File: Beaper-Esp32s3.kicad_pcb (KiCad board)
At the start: 2 copper layers, 65.5 x 100 mm, 98 parts, among them CON1 Phoenix 1729160, J1 Digital, J2 Analog, J3 Conn_01x08, J4 QWIIC/JST SH, Q1 LTR-4206E, Q2 LTR-4206E, Q3 LTR-4206E, Q4 TEPT4400, SW1 RESET, SW2 SW_Push, SW3 SW_Push, SW4 SW_Push, SW5 SW_Push, U1 LM2940T-5.0, U2 74HCT541, U3 SN754410NE, U4 MCP9700A-E/TO

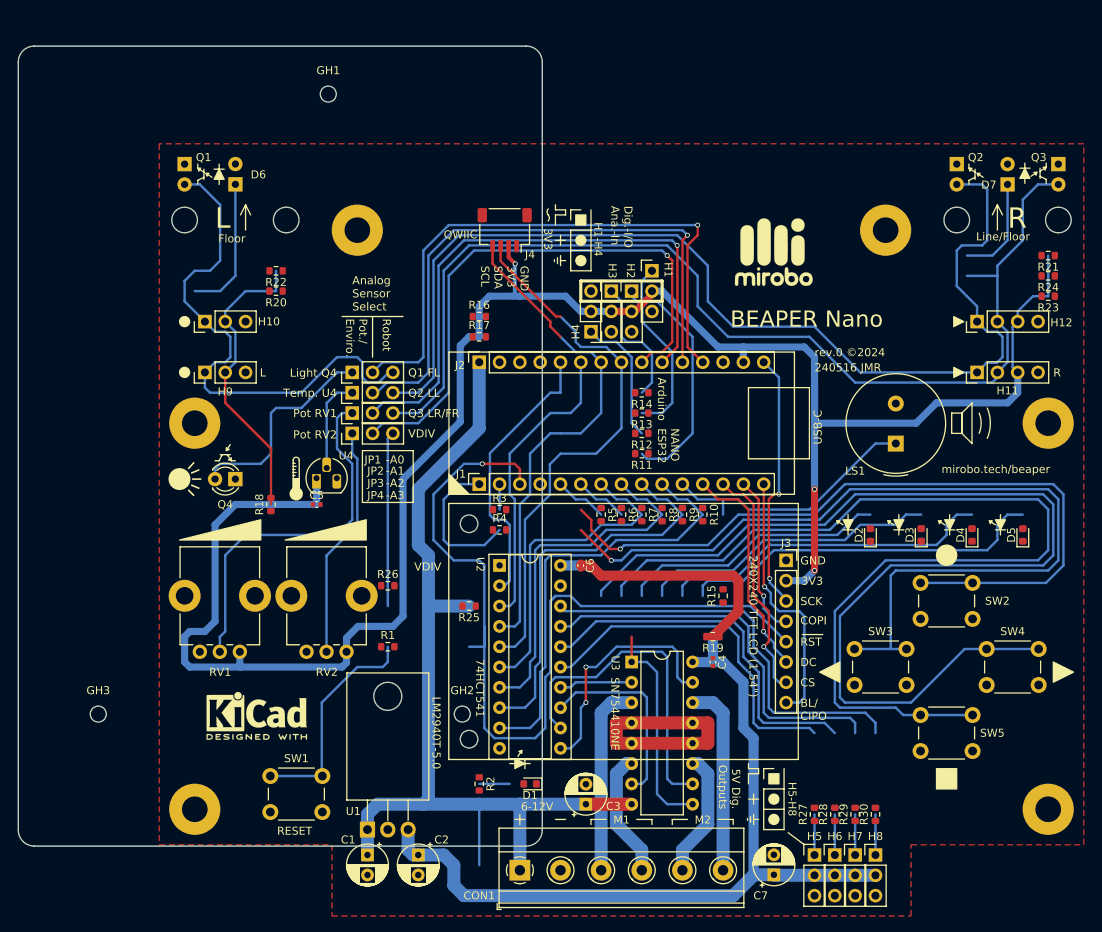
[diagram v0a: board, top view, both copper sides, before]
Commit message: Ajout des jst-ph, ajustement des positions, headers i2c
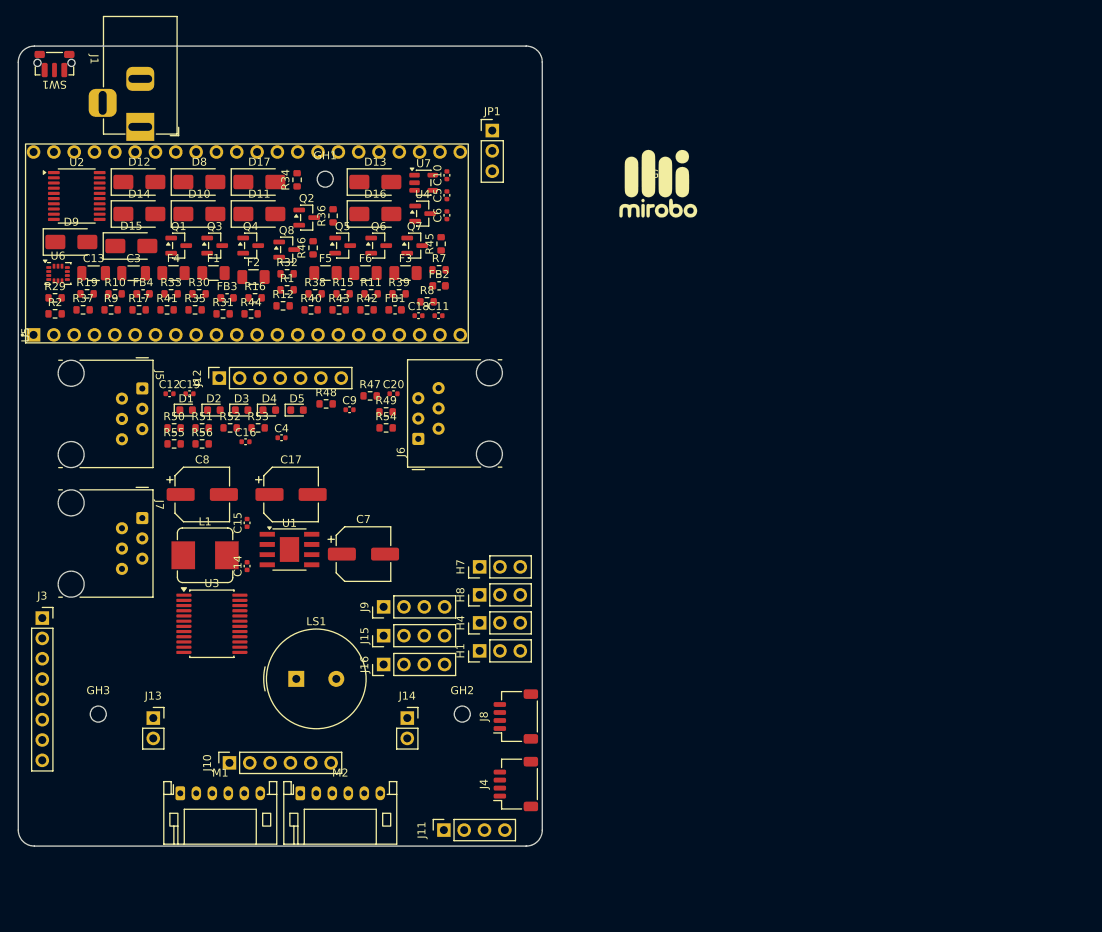
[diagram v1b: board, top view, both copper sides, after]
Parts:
- removed C1, C2: 10uF, Capacitor_THT:CP_Radial_D5.0mm_P2.50mm
- removed CON1: Phoenix 1729160, TerminalBlock_Phoenix:TerminalBlock_Phoenix_MKDS-1,5-6-5.08_1x06_P5.08mm_Horizontal
- removed D6, D7: OED-EL-1L2, BEAPER-Nano:LED_D5.0mm_Clear
- removed H10, H9: Conn_01x03_Male, Connector_PinHeader_2.54mm:PinHeader_1x03_P2.54mm_Vertical
- removed H11, H12: Conn_01x04_Pin, Connector_PinHeader_2.54mm:PinHeader_1x04_P2.54mm_Vertical
- removed H2: A6 (SONAR TRIG), Connector_PinHeader_2.54mm:PinHeader_1x03_P2.54mm_Vertical
- removed H3: A7 (SONAR ECHO), Connector_PinHeader_2.54mm:PinHeader_1x03_P2.54mm_Vertical
- removed H5: A4 (Servo 1), Connector_PinHeader_2.54mm:PinHeader_1x03_P2.54mm_Vertical
- removed H6: A5 (Servo 2), Connector_PinHeader_2.54mm:PinHeader_1x03_P2.54mm_Vertical
- removed J2: Analog, Connector_PinSocket_2.54mm:PinSocket_1x15_P2.54mm_Vertical
- removed JP2: ALS/LFS, Connector_PinHeader_2.54mm:PinHeader_1x03_P2.54mm_Vertical
- removed JP3, JP4: POT/VDIV, Connector_PinHeader_2.54mm:PinHeader_1x03_P2.54mm_Vertical
- removed R13, R14, R20, R21, R27, R28: 100, Resistor_SMD:R_0603_1608Metric
- removed R18, R22, R23, R24: 4k7, Resistor_SMD:R_0603_1608Metric
- removed R25: 5.62k-1%, Resistor_SMD:R_0603_1608Metric
- removed R26: 1.37k-1%, Resistor_SMD:R_0603_1608Metric
- removed R3, R4, R5, R6: 1k0, Resistor_SMD:R_0603_1608Metric
- removed REF**: KiCad-Logo2_5mm_SilkScreen, Symbol:KiCad-Logo2_5mm_SilkScreen
- removed REF** (x6): MountingHole_3.2mm_M3_Pad, MountingHole:MountingHole_3.2mm_M3_Pad
- removed REF** (x4): MountingHole_3.2mm_M3, MountingHole:MountingHole_3.2mm_M3
- removed REF** (x2): MountingHole_2.2mm_M2, MountingHole:MountingHole_2.2mm_M2
- removed RV1, RV2: 10k, Potentiometer_THT:Potentiometer_Bourns_PTV09A-1_Single_Vertical
- removed SW2, SW3, SW4, SW5: SW_Push, Button_Switch_THT:SW_PUSH_6mm
- added C10: 100nF, Capacitor_SMD:C_0402_1005Metric, F.Cu at (103.6, 46.1)
- added C11: 1uF, Capacitor_SMD:C_0402_1005Metric, F.Cu at (102.5, 63.7)
- added C12: 100nF, Capacitor_SMD:C_0402_1005Metric, F.Cu at (68.9, 73.5)
- added C13: 10uF/50V, Capacitor_SMD:C_1206_3216Metric, F.Cu at (59.4, 58.4)
- added C14: 100nF, Capacitor_SMD:C_0402_1005Metric, F.Cu at (78.6, 95.0)
- added C15: 100nF, Capacitor_SMD:C_0402_1005Metric, F.Cu at (78.6, 89.6)
- added C16: 10nF, Capacitor_SMD:C_0402_1005Metric, F.Cu at (78.4, 79.5)
- added C17: 470uF/16V, Capacitor_SMD:CP_Elec_6.3x7.7, F.Cu at (84.1, 86.0)
- added C18: 100nF, Capacitor_SMD:C_0402_1005Metric, F.Cu at (100.0, 63.7)
- added C19: 120pF, Capacitor_SMD:C_0402_1005Metric, F.Cu at (71.4, 73.5)
- added C20: 68pF, Capacitor_SMD:C_0402_1005Metric, F.Cu at (96.9, 73.5)
- added C8: 470uF/16V, Capacitor_SMD:CP_Elec_6.3x7.7, F.Cu at (73.0, 86.0)
- added C9: 100nF, Capacitor_SMD:C_0402_1005Metric, F.Cu at (91.4, 75.5)
- added D10: SS34, Diode_SMD:D_SMA, F.Cu at (72.6, 51.0)
- added D11: SS34, Diode_SMD:D_SMA, F.Cu at (80.1, 51.0)
- added D12: SMAJ5.0CA, Diode_SMD:D_SMA, F.Cu at (65.1, 47.0)
- added D13: SS34, Diode_SMD:D_SMA, F.Cu at (94.6, 47.0)
- added D14: SMAJ12CA, Diode_SMD:D_SMA, F.Cu at (65.1, 51.0)
- added D15: SMAJ12CA, Diode_SMD:D_SMA, F.Cu at (64.1, 55.0)
- added D16: SMAJ12CA, Diode_SMD:D_SMA, F.Cu at (94.6, 51.0)
- added D17: SMAJ12CA, Diode_SMD:D_SMA, F.Cu at (80.1, 47.0)
- added D8: SS54, Diode_SMD:D_SMA, F.Cu at (72.6, 47.0)
- added D9: SMAJ13CA, Diode_SMD:D_SMA, F.Cu at (56.6, 54.5)
- added F1: 3.5A, Fuse:Fuse_1206_3216Metric, F.Cu at (74.4, 58.4)
- added F2: 3A, Fuse:Fuse_1206_3216Metric, F.Cu at (79.4, 58.9)
- added F3: 1A PTC, Fuse:Fuse_1206_3216Metric, F.Cu at (98.4, 58.4)
- added F4: 1A PTC, Fuse:Fuse_1206_3216Metric, F.Cu at (69.4, 58.4)
- added F5: 1A PTC, Fuse:Fuse_1206_3216Metric, F.Cu at (88.4, 58.4)
- added F6: 1A PTC, Fuse:Fuse_1206_3216Metric, F.Cu at (93.4, 58.4)
- added FB1: 120R/2A, Inductor_SMD:L_0603_1608Metric, F.Cu at (97.1, 63.0)
- added FB2: 120R/2A, Inductor_SMD:L_0603_1608Metric, F.Cu at (102.6, 60.0)
- added FB3: 120R/2A, Inductor_SMD:L_0603_1608Metric, F.Cu at (76.1, 61.5)
- added FB4: 120R/2A, Inductor_SMD:L_0603_1608Metric, F.Cu at (65.6, 61.0)
- added J10: VL53L1X module, Connector_PinSocket_2.54mm:PinSocket_1x06_P2.54mm_Vertical, F.Cu at (76.4, 119.6)
- added J11: OLED I2C, Connector_PinSocket_2.54mm:PinSocket_1x04_P2.54mm_Vertical, F.Cu at (103.2, 128.0)
- added J12: PRGB (Auriga panel module), Connector_PinSocket_2.54mm:PinSocket_1x07_P2.54mm_Vertical, F.Cu at (75.1, 71.5)
- added J13: PG1 (GND support), Connector_PinSocket_2.54mm:PinSocket_1x02_P2.54mm_Vertical, F.Cu at (66.9, 114.0)
- added J14: PG2 (GND support), Connector_PinSocket_2.54mm:PinSocket_1x02_P2.54mm_Vertical, F.Cu at (98.6, 114.0)
- added J15: I2C (GND 3V3 SCL SDA), Connector_PinHeader_2.54mm:PinHeader_1x04_P2.54mm_Vertical, F.Cu at (95.7, 103.7)
- added J16: I2C (GND 3V3 SCL SDA), Connector_PinHeader_2.54mm:PinHeader_1x04_P2.54mm_Vertical, F.Cu at (95.7, 107.3)
- added J5: RJ25 port A, Connector_RJ:RJ12_Amphenol_54601-x06_Horizontal, F.Cu at (65.5, 72.8)
- added J6: RJ25 port B, Connector_RJ:RJ12_Amphenol_54601-x06_Horizontal, F.Cu at (100.0, 79.1)
- added J7: RJ25 port C, Connector_RJ:RJ12_Amphenol_54601-x06_Horizontal, F.Cu at (65.5, 89.0)
- added J8: QWIIC/JST SH, Connector_JST:JST_SH_SM04B-SRSS-TB_1x04-1MP_P1.00mm_Horizontal, F.Cu at (112.2, 113.8)
- added J9: I2C (GND 3V3 SCL SDA), Connector_PinHeader_2.54mm:PinHeader_1x04_P2.54mm_Vertical, F.Cu at (95.7, 100.1)
- added L1: 6.8uH/4.5A, Inductor_SMD:L_Bourns_SRP7028A_7.3x6.6mm, F.Cu at (73.3, 93.7)
- added M1: Moteur 1 (MHDR1X6), Connector_JST:JST_PH_S6B-PH-K_1x06_P2.00mm_Horizontal, F.Cu at (70.2, 123.4)
- added M2: Moteur 2 (MHDR1X6), Connector_JST:JST_PH_S6B-PH-K_1x06_P2.00mm_Horizontal, F.Cu at (85.2, 123.4)
- added Q5: BSS138, Package_TO_SOT_SMD:SOT-23, F.Cu at (90.5, 54.9)
- added Q6: BSS138, Package_TO_SOT_SMD:SOT-23, F.Cu at (95.0, 54.9)
- added Q7: BSS138, Package_TO_SOT_SMD:SOT-23, F.Cu at (99.5, 54.9)
- added Q8: BSS138, Package_TO_SOT_SMD:SOT-23, F.Cu at (83.5, 55.4)
- added R31: 51, Resistor_SMD:R_0603_1608Metric, F.Cu at (75.6, 63.5)
- added R32: 51, Resistor_SMD:R_0603_1608Metric, F.Cu at (83.6, 58.5)
- added R33: 51, Resistor_SMD:R_0603_1608Metric, F.Cu at (69.1, 61.0)
- added R34: 51, Resistor_SMD:R_0603_1608Metric, F.Cu at (84.8, 46.7)
- added R35: 100k, Resistor_SMD:R_0603_1608Metric, F.Cu at (72.1, 63.0)
- added R36: 51k, Resistor_SMD:R_0603_1608Metric, F.Cu at (89.3, 51.2)
- added R37: 10k, Resistor_SMD:R_0603_1608Metric, F.Cu at (58.1, 63.0)
- added R38: 15k, Resistor_SMD:R_0603_1608Metric, F.Cu at (87.1, 61.0)
- added R39: 220, Resistor_SMD:R_0603_1608Metric, F.Cu at (97.6, 61.0)
- added R40: 10k, Resistor_SMD:R_0603_1608Metric, F.Cu at (86.6, 63.0)
- added R41: 1.91k, Resistor_SMD:R_0603_1608Metric, F.Cu at (68.6, 63.0)
- added R42: 30k, Resistor_SMD:R_0603_1608Metric, F.Cu at (93.6, 63.0)
- added R43: 4.7k, Resistor_SMD:R_0603_1608Metric, F.Cu at (90.1, 63.0)
- added R44: 4.7k, Resistor_SMD:R_0603_1608Metric, F.Cu at (79.1, 63.5)
- added R45: 10k, Resistor_SMD:R_0603_1608Metric, F.Cu at (102.8, 54.7)
- added R46: 10k, Resistor_SMD:R_0603_1608Metric, F.Cu at (86.8, 55.2)
- added R47: 10k, Resistor_SMD:R_0603_1608Metric, F.Cu at (94.0, 73.7)
- added R48: 10k, Resistor_SMD:R_0603_1608Metric, F.Cu at (88.5, 74.7)
- added R49: 10k, Resistor_SMD:R_0603_1608Metric, F.Cu at (96.0, 75.7)
- added R50: 10k, Resistor_SMD:R_0603_1608Metric, F.Cu at (69.5, 77.7)
- added R51: 10k, Resistor_SMD:R_0603_1608Metric, F.Cu at (73.0, 77.7)
- added R52: 10k, Resistor_SMD:R_0603_1608Metric, F.Cu at (76.5, 77.7)
- added R53: 10k, Resistor_SMD:R_0603_1608Metric, F.Cu at (80.0, 77.7)
- added R54: 10k, Resistor_SMD:R_0603_1608Metric, F.Cu at (96.0, 77.7)
- added R55: 10k, Resistor_SMD:R_0603_1608Metric, F.Cu at (69.5, 79.7)
- added R56: 10k, Resistor_SMD:R_0603_1608Metric, F.Cu at (73.0, 79.7)
- added U5: ESP32-S3-DevKitC-1-N16R8, BEAPER-Nano:ESP32-S3-DevKitC-1, F.Cu at (51.9, 66.1)
- added U6: LSM6DS3TR-C, Package_LGA:LGA-14_3x2.5mm_P0.5mm_LayoutBorder3x4y, F.Cu at (55.0, 58.4)
- added U7: 74AHCT1G125, Package_TO_SOT_SMD:SOT-23-5, F.Cu at (100.7, 47.1)
- C3: value 10uF -> 10uF/50V; footprint Capacitor_THT:CP_Radial_D5.0mm_P2.50mm -> Capacitor_SMD:C_1206_3216Metric
- C7: value 10uF -> 470uF/16V; footprint Capacitor_THT:CP_Radial_D5.0mm_P2.50mm -> Capacitor_SMD:CP_Elec_6.3x7.7
- J1: value Digital -> DC jack 5.5x2.1; footprint Connector_PinSocket_2.54mm:PinSocket_1x15_P2.54mm_Vertical -> Connector_BarrelJack:BarrelJack_Horizontal
- JP1: value ALS/LFS -> I2C EXT 3V3/5V
- Q1, Q2, Q3: value LTR-4206E -> BSS138; footprint BEAPER-Nano:LED_D3.0mm_IRBlack -> Package_TO_SOT_SMD:SOT-23; moved to F.Cu
- Q4: value TEPT4400 -> BSS138; footprint BEAPER-Nano:LED_D3.0mm_Clear -> Package_TO_SOT_SMD:SOT-23
- SW1: footprint Button_Switch_THT:SW_PUSH_6mm -> Button_Switch_SMD:SW_Push_1P1T-MP_NO_Horizontal_Alps_SKRTLAE010
- U1: value LM2940T-5.0 -> TPS54331DDA; footprint Package_TO_SOT_THT:TO-220-3_Horizontal_TabDown -> Package_SO:TI_SO-PowerPAD-8
- U2: footprint Package_DIP:DIP-20_W7.62mm_Socket -> Package_SO:TSSOP-20_4.4x6.5mm_P0.65mm
- U3: value SN754410NE -> TB6612FNG; footprint Package_DIP:DIP-16_W7.62mm -> Package_SO:SSOP-24_5.3x8.2mm_P0.65mm
- U4: value MCP9700A-E/TO -> MCP9700AT-E/TT; footprint Package_TO_SOT_THT:TO-92_HandSolder -> Package_TO_SOT_SMD:SOT-23
- moved R29 119.0 mm to (54.6, 61.5), turned to 0 degrees
- moved R30 106.7 mm to (72.6, 61.0), turned to 0 degrees
- moved Q3 105.7 mm to (74.5, 54.9), turned to 0 degrees
- moved SW1 99.5 mm to (54.5, 32.1)
- moved J3 93.3 mm to (53.0, 101.5)
- moved D5 92.1 mm to (84.8, 75.5), turned to 0 degrees
- moved D4 89.2 mm to (81.4, 75.5), turned to 0 degrees
- moved R19 89.2 mm to (58.6, 61.0), turned to 0 degrees
- moved C3 87.2 mm to (64.4, 58.4), turned to 0 degrees
- moved D3 86.4 mm to (77.9, 75.5), turned to 0 degrees
- moved D2 83.5 mm to (74.5, 75.5), turned to 0 degrees
- moved Q2 81.4 mm to (86.0, 51.4), turned to 0 degrees
- moved LS1 80.5 mm to (84.8, 109.1), turned to 0 degrees
- moved R2 79.1 mm to (54.6, 63.5), turned to 0 degrees
- moved R10 78.5 mm to (62.1, 61.0), turned to 0 degrees
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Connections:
- J1 pad 1: /D1/TX0 -> /VBAT
- J1 pad 2: /D0/RX0 -> GND
- J1 pad 3: /~{RST} -> (no net)
- JP1 pad 1: Net-(JP1-A) -> +3V3
- JP1 pad 2: /A0 -> /VI2C
- JP1 pad 3: /Q1 -> /5V_P
- Q1 pad 1: /Q1 -> +3V3
- Q1 pad 2: GND -> /A4/SDA
- Q2 pad 1: /Q2 -> +3V3
- Q2 pad 2: GND -> /A5/SCL
- Q3 pad 1: /Q3 -> +3V3
- Q3 pad 2: GND -> /PA_S1
- Q4 pad 1: Net-(JP1-A) -> +3V3
- Q4 pad 2: GND -> /PA_S2
- R19 pad 2: Net-(U3-1,2EN) -> /MOTOR_STBY
- U1 pad 1: VCC -> Net-(U1-BOOT)
- U1 pad 2: GND -> Net-(D13-K)
- U1 pad 3: +5V -> unconnected-(U1-EN-Pad3)
- U2 pad 11: Net-(U2-Y7) -> /M2_IN2
- U2 pad 12: Net-(U2-Y6) -> /M2_IN1
- U2 pad 13: Net-(U2-Y5) -> /M1_IN2
- U2 pad 14: Net-(U2-Y4) -> /M1_IN1
- U2 pad 15: Net-(U2-Y3) -> unconnected-(U2-Y3-Pad15)
- U2 pad 16: Net-(U2-Y2) -> unconnected-(U2-Y2-Pad16)
- U3 pad 1: Net-(U3-1,2EN) -> /M1A_D
- U3 pad 10: Net-(U2-Y6) -> GND
- U3 pad 11: Net-(CON1-Pin_5) -> /M2A_D
- U3 pad 12: GND -> /M2A_D
- U3 pad 13: GND -> VCC
- U3 pad 14: Net-(CON1-Pin_6) -> VCC
- U3 pad 15: Net-(U2-Y7) -> +5V
- U3 pad 16: +5V -> /M2_IN2
- U3 pad 2: Net-(U2-Y4) -> /M1A_D
- U3 pad 3: Net-(CON1-Pin_3) -> GND
- U3 pad 5: GND -> /M1B_D
- U3 pad 6: Net-(CON1-Pin_4) -> /M1B_D
- U3 pad 7: Net-(U2-Y5) -> /M2B_D
- U3 pad 8: VCC -> /M2B_D
- U3 pad 9: Net-(U3-1,2EN) -> GND
- U4 pad 2: Net-(JP2-A) -> /A1
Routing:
- net +3V3: track 292.1 -> 0.00 mm, vias 3 -> 0
- net Net-(R5-Pad2): track 136.9 -> 0.00 mm
- net /Q3: track 136.0 -> 0.00 mm
- net /Q2: track 134.6 -> 0.00 mm
- net +5V: track 132.4 -> 0.00 mm
- net Net-(R6-Pad2): track 123.8 -> 0.00 mm
- net VCC: track 119.4 -> 0.00 mm
- net Net-(R4-Pad2): track 110.5 -> 0.00 mm, vias 1 -> 0
- net /~{RST}: track 110.3 -> 0.00 mm, vias 1 -> 0
- net Net-(R3-Pad2): track 94.6 -> 0.00 mm, vias 1 -> 0
- net /A0: track 74.5 -> 0.00 mm, vias 1 -> 0
- net /A1: track 72.7 -> 0.00 mm, vias 1 -> 0
- net /A2: track 71.2 -> 0.00 mm, vias 1 -> 0
- net /A3: track 71.0 -> 0.00 mm, vias 1 -> 0
- net /A4/SDA: track 68.5 -> 0.00 mm
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- removed copper zone on F.Cu, net GND
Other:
- board text removed: "-A0"
- board text removed: "-A1"
- board text removed: "-A2"
- board text removed: "-A3"
- board text removed: "240516 JMR"
- board text removed: "240X240 TFT LCD (1.54{dblquote})"
- board text removed: "3V3"
- board text removed: "5V Dig. Outputs"
- board text removed: "6-12V"
- board text removed: "74HCT541"
- board text removed: "A0/1"
- board text removed: "A1/2"
- board text removed: "A2/3"
- board text removed: "A3"
- board text removed: "A4/11"
- board text removed: "A5/12"
- board text removed: "A6/13"
- board text removed: "A7"
- board text removed: "Analog Sensor Select"
- board text removed: "Arduino"
- board text removed: "B0/46"
- board text removed: "B1/0"
- board text removed: "BEAPER Nano"
- board text removed: "BL/ CIPO"
- board text removed: "BL/CIPO"
- board text removed: "COPI"
- board text removed: "CS"
- board text removed: "D0/44"
- board text removed: "D1/43"
- board text removed: "D10/21"
- board text removed: "D11/38"
- board text removed: "D12/47"
- board text removed: "D13/48"
- board text removed: "D2"
- board text removed: "D3"
- board text removed: "D3/6"
- board text removed: "D4"
- board text removed: "D4/7"
- board text removed: "D5"
- board text removed: "D5/8"
- board text removed: "D6"
- board text removed: "D7"
- board text removed: "D7/10"
- board text removed: "D8/17"
- board text removed: "D9/18"
- board text removed: "DC"
- board text removed: "Dig.-I/O Ana.-In"
- board text removed: "Floor"
- board text removed: "GND"
- board text removed: "GND 3V3 SDA SCL"
- board text removed: "H1"
- board text removed: "H1-H4"
- board text removed: "H2"
- board text removed: "H3"
- board text removed: "H4"
- board text removed: "H5"
- board text removed: "H5-H8"
- board text removed: "H6"
- board text removed: "H7"
- board text removed: "H8"
- board text removed: "L"
- board text removed: "LM2940T-5.0"
- board text removed: "Light Q4"
- board text removed: "Line/Floor"
- board text removed: "M1"
- board text removed: "M2"
- board text removed: "NANO ESP32"
- board text removed: "Pot RV1"
- board text removed: "Pot RV2"
- board text removed: "Pot./ Enviro."
- board text removed: "Q1"
- board text removed: "Q1 FL"
- board text removed: "Q2"
- board text removed: "Q2 LL"
- board text removed: "Q3"
- board text removed: "Q3 LR/FR"
- board text removed: "QWIIC"
- board text removed: "R"
- board text removed: "RESET"
- board text removed: "RST"
- board text removed: "Robot"
- board text removed: "SCK"
- board text removed: "SN754410NE"
- board text removed: "SW2"
- board text removed: "SW3"
- board text removed: "SW4"
- board text removed: "SW5"
- board text removed: "Temp. U4"
- board text removed: "USB-C"
- board text removed: "VBUS"
- board text removed: "VDIV"
- board text removed: "VIN"
- board text removed: "mirobo.tech/beaper"
- board text removed: "rev.0 ©2024"

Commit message: Déplacement majeur
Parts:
- moved J11 76.4 mm to (52.2, 71.1), turned to 0 degrees
- moved R34 71.6 mm to (91.8, 118.0)
- moved C10 68.2 mm to (61.8, 100.0)
- moved D16 63.7 mm to (85.5, 114.0)
- moved D17 63.6 mm to (85.5, 110.4)
- moved D14 63.2 mm to (70.0, 114.0)
- moved R33 62.1 mm to (93.6, 118.0), turned to 90 degrees
- moved R32 60.5 mm to (70.2, 117.5), turned to 90 degrees
- moved F3 58.9 mm to (79.0, 114.0)
- moved FB2 57.4 mm to (75.2, 110.4)
- moved F5 56.0 mm to (94.8, 114.0)
- moved D15 55.7 mm to (70.0, 110.4)
- moved FB4 55.6 mm to (91.0, 110.4)
- moved FB1 55.5 mm to (75.2, 114.0)
- moved R36 54.8 mm to (97.6, 105.4), turned to 0 degrees
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
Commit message: candidat pour pièces bien placées
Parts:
- moved R43 58.1 mm to (106.2, 46.6)
- moved R7 51.9 mm to (55.8, 100.6), turned to 90 degrees
- moved R8 51.3 mm to (52.2, 100.6), turned to 90 degrees
- moved D13 47.6 mm to (101.8, 101.1)
- moved R53 41.4 mm to (95.8, 90.6), turned to 0 degrees
- moved C11 40.6 mm to (86.8, 65.1), turned to 90 degrees
- moved Q8 39.5 mm to (53.8, 91.6)
- moved R29 35.9 mm to (60.8, 67.1)
- moved R10 35.5 mm to (67.8, 67.1)
- moved R19 35.5 mm to (64.2, 67.1)
- moved R2 35.2 mm to (57.2, 70.3)
- moved R17 34.8 mm to (67.8, 70.3)
- moved R37 34.8 mm to (60.8, 70.3)
- moved R9 34.8 mm to (64.2, 70.3)
- moved R35 31.5 mm to (87.8, 74.6)
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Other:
- board text added: "3V3"
- board text added: "5V"
- board text added: "GND"
- board text added: "IO0"
- board text added: "IO1"
- board text added: "IO10"
- board text added: "IO11"
- board text added: "IO12"
- board text added: "IO13"
- board text added: "IO14"
- board text added: "IO15"
- board text added: "IO16"
- board text added: "IO17"
- board text added: "IO18"
- board text added: "IO19"
- board text added: "IO2"
- board text added: "IO20"
- board text added: "IO21"
- board text added: "IO3"
- board text added: "IO35"
- board text added: "IO36"
- board text added: "IO37"
- board text added: "IO38"
- board text added: "IO39"
- board text added: "IO4"
- board text added: "IO40"
- board text added: "IO41"
- board text added: "IO42"
- board text added: "IO45"
- board text added: "IO46"
- board text added: "IO47"
- board text added: "IO48"
- board text added: "IO5"
- board text added: "IO6"
- board text added: "IO7"
- board text added: "IO8"
- board text added: "IO9"
- board text added: "RST"
- board text added: "RX"
- board text added: "TX"

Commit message: Candidat avec J4 et J8 déplacé
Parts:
- U5: footprint BEAPER-Nano:ESP32-S3-DevKitC-1 -> BEAPER-Nano:ESP32-S3-DevKitC-1-2x22
- moved J4 79.7 mm to (67.2, 33.6), turned to 180 degrees
- moved J8 58.3 mm to (53.2, 85.6), turned to -90 degrees
- moved U5 58.0 mm to (113.9, 84.4), turned to -90 degrees
- moved R48 46.8 mm to (105.8, 97.6)
- moved R15 40.1 mm to (68.8, 102.1)
- moved Q7 33.6 mm to (98.8, 96.6)
- moved R47 33.2 mm to (89.8, 63.6)
- moved Q5 31.5 mm to (93.2, 65.6)
- moved R33 30.5 mm to (67.8, 113.1)
- moved R34 30.5 mm to (64.8, 113.1)
- moved SW1 29.7 mm to (95.8, 32.6)
- moved R55 19.1 mm to (52.2, 97.1), turned to 90 degrees
- moved FB3 19.1 mm to (71.2, 113.6)
- moved F6 16.3 mm to (79.2, 116.6)
- moved FB4 16.2 mm to (75.2, 116.6)
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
